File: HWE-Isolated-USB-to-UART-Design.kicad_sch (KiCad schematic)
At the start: 0 parts

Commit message: Research Phase 85% done, with USB Type C, USB-to-UART IC, and Digital Isolator Researched & Selected, but will close eevrything once validated everything by going through datasheets of the component IC
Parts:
- added J1: USB_C_Receptacle_USB2.0_16P, Connector_USB:USB_C_Receptacle_HRO_TYPE-C-31-M-12, symbol Connector:USB_C_Receptacle_USB2.0_16P
- added U1: CP2102N-Axx-xQFN24, Package_DFN_QFN:QFN-24-1EP_4x4mm_P0.5mm_EP2.6x2.6mm, symbol Interface_USB:CP2102N-Axx-xQFN24
- added U2: ISO7762FDBQ, Package_SO:SSOP-16_3.9x4.9mm_P0.635mm, symbol Isolator:ISO7762FDBQ
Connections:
- new net: J1.A1 (GND), J1.A12 (GND), J1.B1 (GND), J1.B12 (GND)
- new net: J1.A4 (VBUS), J1.A9 (VBUS), J1.B4 (VBUS), J1.B9 (VBUS)
- new net: U1.2 (GND), U1.25 (GND)

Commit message: deep diving into the component datasheets for USB Type C Connector and USB UART IC -WIP
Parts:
- added U3: USBLC6-2SC6, Package_TO_SOT_SMD:SOT-23-6_Handsoldering, symbol Power_Protection:USBLC6-2SC6
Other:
- moved on the sheet: J1, U1, U2
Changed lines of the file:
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@@
 	(symbol
 		(lib_id "Connector:USB_C_Receptacle_USB2.0_16P")
-		(at 35.56 55.88 0)
+		(at 40.64 59.69 0)
 		(unit 1)
 		(body_style 1)
@@
 		(fields_autoplaced yes)
 		(property "Reference" "J1"
-			(at 35.56 33.02 0)
+			(at 40.64 36.83 0)
 			(show_name no)
 			(do_not_autoplace no)
@@
 		)
 		(property "Value" "USB_C_Receptacle_USB2.0_16P"
-			(at 35.56 35.56 0)
+			(at 40.64 39.37 0)
 			(show_name no)
 			(do_not_autoplace no)
@@
 		)
 		(property "Footprint" "Connector_USB:USB_C_Receptacle_HRO_TYPE-C-31-M-12"
-			(at 39.37 55.88 0)
+			(at 44.45 59.69 0)
 			(hide yes)
 			(show_name no)
@@
 		)
 		(property "Datasheet" "https://www.usb.org/sites/default/files/documents/usb_type-c.zip"
-			(at 39.37 55.88 0)
+			(at 44.45 59.69 0)
 			(hide yes)
 			(show_name no)
@@
 		)
 		(property "Description" "USB 2.0-only 16P Type-C Receptacle connector"
-			(at 35.56 55.88 0)
+			(at 40.64 59.69 0)
 			(hide yes)
 			(show_name no)
@@
 	(symbol
 		(lib_id "Isolator:ISO7762FDBQ")
-		(at 140.97 68.58 0)
+		(at 161.29 59.69 0)
 		(unit 1)
 		(body_style 1)
@@
 		(fields_autoplaced yes)
 		(property "Reference" "U2"
-			(at 148.1933 48.26 0)
+			(at 168.5133 39.37 0)
 			(show_name no)
 			(do_not_autoplace no)
@@
 		)
 		(property "Value" "ISO7762FDBQ"
-			(at 148.1933 50.8 0)
+			(at 168.5133 41.91 0)
 			(show_name no)
 			(do_not_autoplace no)
@@
 		)
 		(property "Footprint" "Package_SO:SSOP-16_3.9x4.9mm_P0.635mm"
-			(at 146.685 82.55 0)
+			(at 167.005 73.66 0)
 			(hide yes)
 			(show_name no)
@@
 		)
 		(property "Datasheet" "https://www.ti.com/lit/ds/symlink/iso7763.pdf?ts=1596905577895"
-			(at 151.13 71.12 0)
+			(at 171.45 62.23 0)
 			(hide yes)
 			(show_name no)
@@
 		)
 		(property "Description" "Default low, High-speed, robust EMC, reinforced, six-channel, digital, isolator, SSOP-16"
-			(at 140.97 68.58 0)
+			(at 161.29 59.69 0)
 			(hide yes)
 			(show_name no)
@@
 	)
 	(symbol
+		(lib_id "Power_Protection:USBLC6-2SC6")
+		(at 74.93 77.47 0)
+		(unit 1)
+		(body_style 1)
+		(exclude_from_sim no)
+		(in_bom yes)
+		(on_board yes)
+		(in_pos_files yes)
+		(dnp no)
+		(fields_autoplaced yes)
+		(property "Reference" "U3"
+			(at 76.5811 69.85 0)
+			(show_name no)
+			(do_not_autoplace no)
+			(effects
+				(font
+					(size 1.27 1.27)
+				)
+				(justify left)
+			)
+		)
+		(property "Value" "USBLC6-2SC6"
+			(at 76.5811 72.39 0)
+			(show_name no)
+			(do_not_autoplace no)
+			(effects
+				(font
+					(size 1.27 1.27)
+				)
+				(justify left)
+			)
+		)
+		(property "Footprint" "Package_TO_SOT_SMD:SOT-23-6_Handsoldering"
+			(at 76.2 83.82 0)
+			(hide yes)
+			(show_name no)
+			(do_not_autoplace no)
+			(effects
+				(font
+					(size 1.27 1.27)
+					(italic yes)
+				)
+				(justify left)
+			)
+		)
+		(property "Datasheet" "https://www.st.com/resource/en/datasheet/usblc6-2.pdf"
+			(at 76.2 85.725 0)
+			(hide yes)
+			(show_name no)
+			(do_not_autoplace no)
+			(effects
+				(font
+					(size 1.27 1.27)
+				)
+				(justify left)
+			)
+		)
+		(property "Description" "Very low capacitance ESD protection diode, 2 data-line, SOT-23-6"
+			(at 74.93 77.47 0)
+			(hide yes)
+			(show_name no)
+			(do_not_autoplace no)
+			(effects
+				(font
+					(size 1.27 1.27)
+				)
+			)
+		)
+		(pin "2"
+		)
+		(pin "1"
+		)
+		(pin "3"
+		)
+		(pin "5"
+		)
+		(pin "6"
+		)
+		(pin "4"
+		)
+		(instances
+			(project "HWE-Isolated-USB-to-UART-Design"
+				(path "/b7bfdaa0-038f-4b80-877f-94c6e9c4db2c"
+					(reference "U3")
+					(unit 1)
+				)
+			)
+		)
+	)
+	(symbol
 		(lib_id "Interface_USB:CP2102N-Axx-xQFN24")
-		(at 85.09 67.31 0)
+		(at 114.3 60.96 0)
 		(unit 1)
 		(body_style 1)
@@
 		(fields_autoplaced yes)
 		(property "Reference" "U1"
-			(at 87.2333 95.25 0)
+			(at 116.4433 88.9 0)
 			(show_name no)
 			(do_not_autoplace no)
@@
 		)
 		(property "Value" "CP2102N-Axx-xQFN24"
-			(at 87.2333 97.79 0)
+			(at 116.4433 91.44 0)
 			(show_name no)
 			(do_not_autoplace no)
@@
 		)
 		(property "Footprint" "Package_DFN_QFN:QFN-24-1EP_4x4mm_P0.5mm_EP2.6x2.6mm"
-			(at 116.84 93.98 0)
+			(at 146.05 87.63 0)
 			(hide yes)
 			(show_name no)
@@
 		)
 		(property "Datasheet" "https://www.silabs.com/documents/public/data-sheets/cp2102n-datasheet.pdf"
-			(at 86.36 86.36 0)
+			(at 115.57 80.01 0)
 			(hide yes)
 			(show_name no)
@@
 		)
 		(property "Description" "USB to UART master bridge, QFN-24"
-			(at 85.09 67.31 0)
-			(hide yes)
-			(show_name no)
+			(at 114.3 60.96 0)
+			(hide yes)
+			(show_name no)

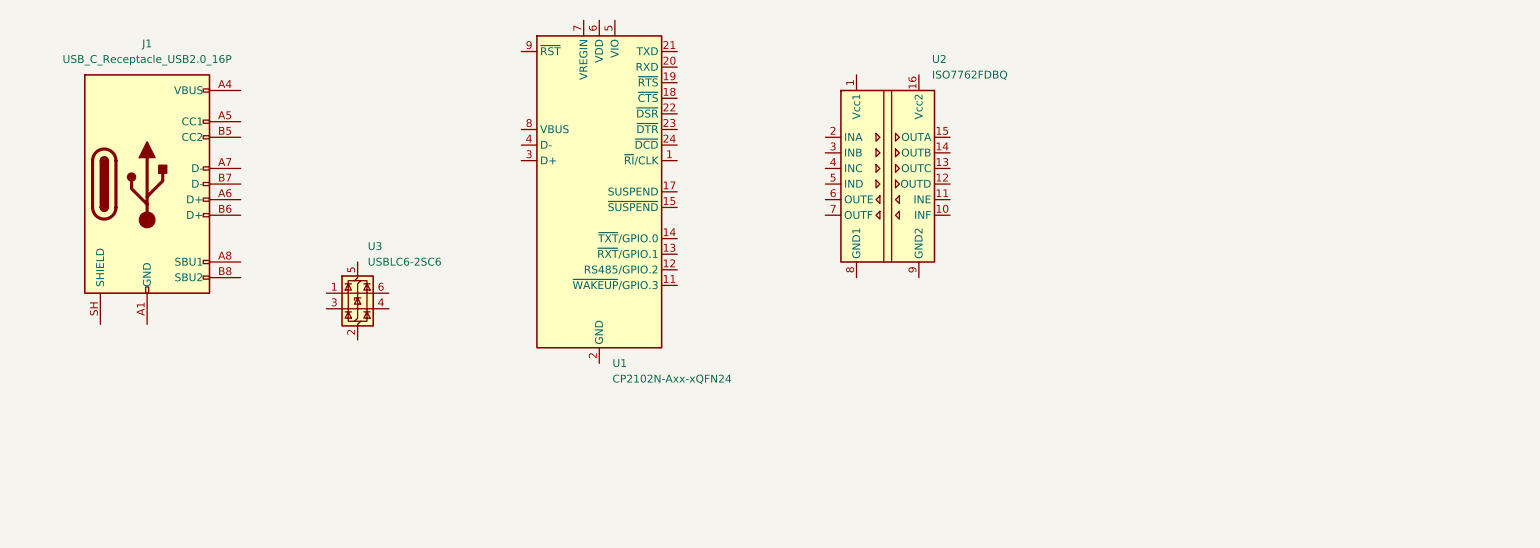
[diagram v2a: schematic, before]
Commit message: Currently in Schematic Design phase, just finished with draft usb c design, and now setup done for SP2102N & Digital Isolator Section
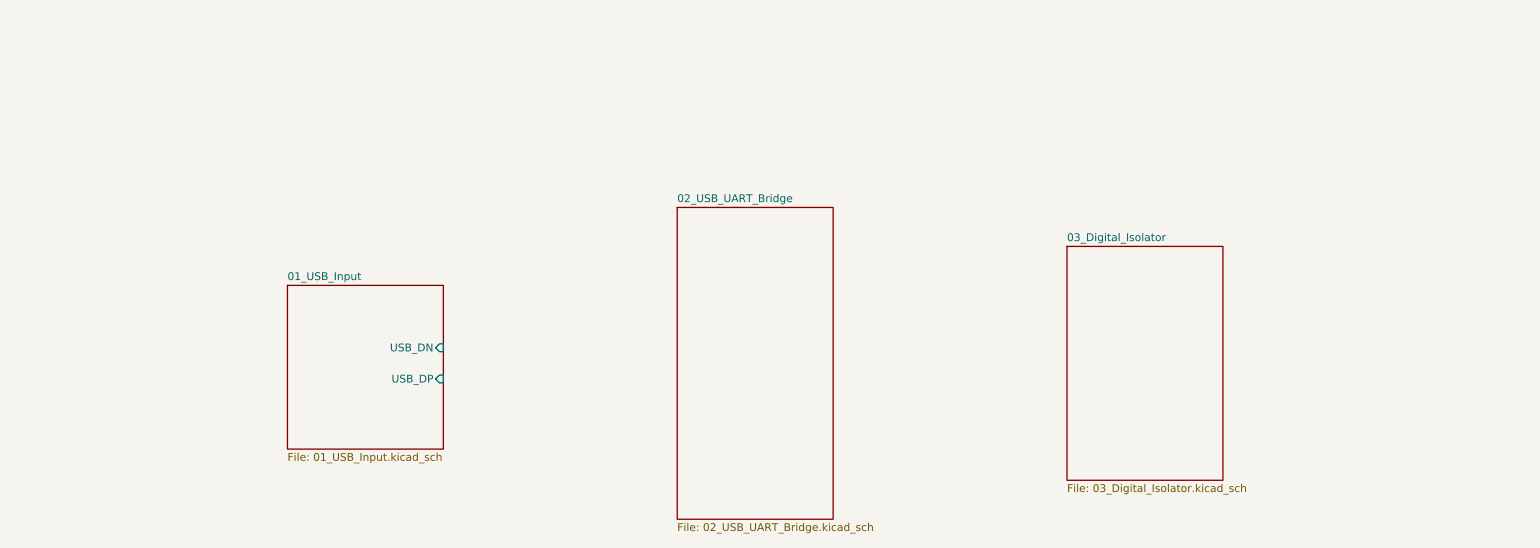
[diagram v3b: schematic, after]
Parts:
- removed J1: USB_C_Receptacle_USB2.0_16P, Connector_USB:USB_C_Receptacle_HRO_TYPE-C-31-M-12, symbol Connector:USB_C_Receptacle_USB2.0_16P
- removed U1: CP2102N-Axx-xQFN24, Package_DFN_QFN:QFN-24-1EP_4x4mm_P0.5mm_EP2.6x2.6mm, symbol Interface_USB:CP2102N-Axx-xQFN24
- removed U2: ISO7762FDBQ, Package_SO:SSOP-16_3.9x4.9mm_P0.635mm, symbol Isolator:ISO7762FDBQ
- removed U3: USBLC6-2SC6, Package_TO_SOT_SMD:SOT-23-6_Handsoldering, symbol Power_Protection:USBLC6-2SC6
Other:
- added sheet 01_USB_Input (01_USB_Input.kicad_sch)
- added sheet 02_USB_UART_Bridge (02_USB_UART_Bridge.kicad_sch)
- added sheet 03_Digital_Isolator (03_Digital_Isolator.kicad_sch)
- title: (none) -> Isolated USB to UART Module Design

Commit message: completed schematic design, and selected all footprints and for now will go for 0805 for resistors, capacitors and leds - will later make a call during layoting
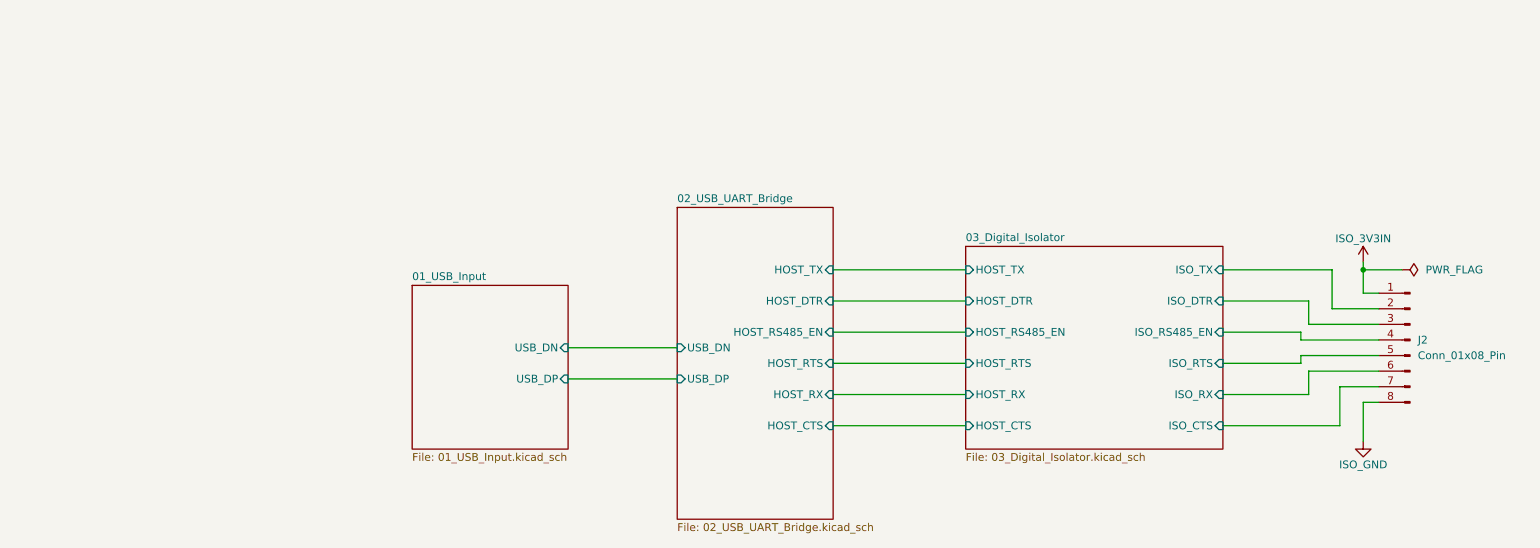
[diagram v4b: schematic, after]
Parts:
- added J2: Conn_01x08_Pin, Connector_PinHeader_2.54mm:PinHeader_1x08_P2.54mm_Horizontal, symbol Connector:Conn_01x08_Pin
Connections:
- new net 03_Digital_Isolator/ISO_CTS: J2.7 (Pin_7)
- new net 03_Digital_Isolator/ISO_DTR: J2.3 (Pin_3)
- new net 03_Digital_Isolator/ISO_RS485_EN: J2.4 (Pin_4)
- new net 03_Digital_Isolator/ISO_RTS: J2.5 (Pin_5)
- new net 03_Digital_Isolator/ISO_RX: J2.6 (Pin_6)
- new net 03_Digital_Isolator/ISO_TX: J2.2 (Pin_2)
- new net ISO_3V3IN: J2.1 (Pin_1)
- new net ISO_GND: J2.8 (Pin_8)
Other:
- sheet 02_USB_UART_Bridge ports: added HOST_CTS, HOST_DTR, HOST_RS485_EN, HOST_RTS, HOST_RX, HOST_TX, USB_DN, USB_DP; removed none
- sheet 03_Digital_Isolator ports: added HOST_CTS, HOST_DTR, HOST_RS485_EN, HOST_RTS, HOST_RX, HOST_TX, ISO_CTS, ISO_DTR, ISO_RS485_EN, ISO_RTS, ISO_RX, ISO_TX; removed none
